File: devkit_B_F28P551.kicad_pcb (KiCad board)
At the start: 2 copper layers, 90 x 45 mm, 0 parts

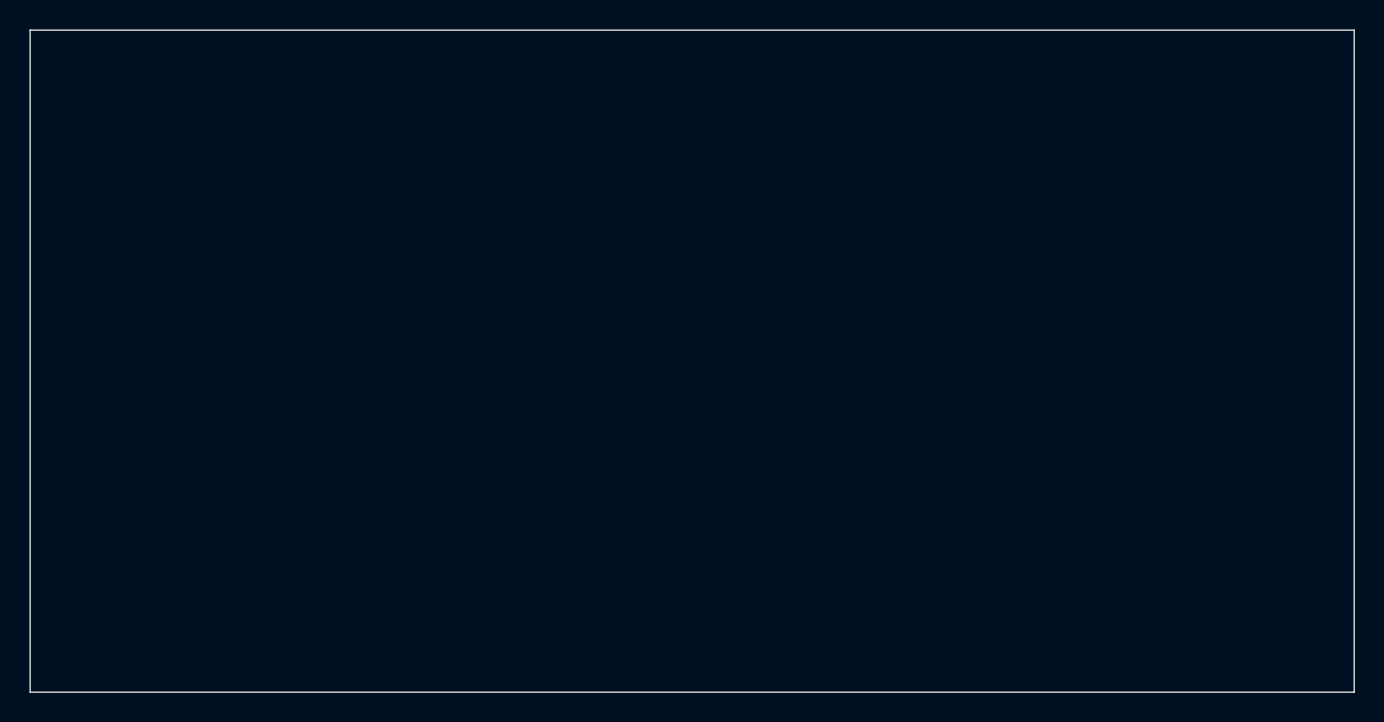
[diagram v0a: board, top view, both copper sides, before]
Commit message: spec-devkit.md devient la source de verite unique, brochage-devkit.md fusionne
La specification consolidee fournie remplace, comme elle l'annonce elle-meme,
tous les documents de brochage anterieurs. Verifiee contre
lib/C2000_Devkit_Connectors.kicad_sym: 56 positions sur 56, zero ecart.

brochage-devkit.md dupliquait desormais les memes 56 positions dans une autre
mise en forme — le mode de defaillance exact qui vient de couter trois semaines
de divergence. Il est reduit a ce qu'il avait d'unique et renomme
nappes-shield.md: les quatre nappes vers la carte de puissance, et la
repartition des cartes.

La specification apporte trois choses absentes du depot: l'entraxe 25,4 mm des
rangees (contre 22,86 mm pour l'ESP32, soit deux references de support sur le
shield), la valeur OTP BOOTPIN_CONFIG = 0x5AFF18FF, et l'obligation d'ecrire
GPIOHAMSEL pour piloter GPIO20/GPIO21 en numerique sur le F28P551.

Le contour du devkit passe de 90 x 45 a 75 x 28 mm: il portait « dimension a
confirmer », elle l'est.

Conflit non tranche, porte dans les points ouverts: la specification recommande
quatre couches pour un plan de masse continu sous la zone analogique, la
contrainte de fabrication du CLAUDE.md en pose deux.

Co-Authored-By: Claude Opus 5 <noreply@anthropic.com>
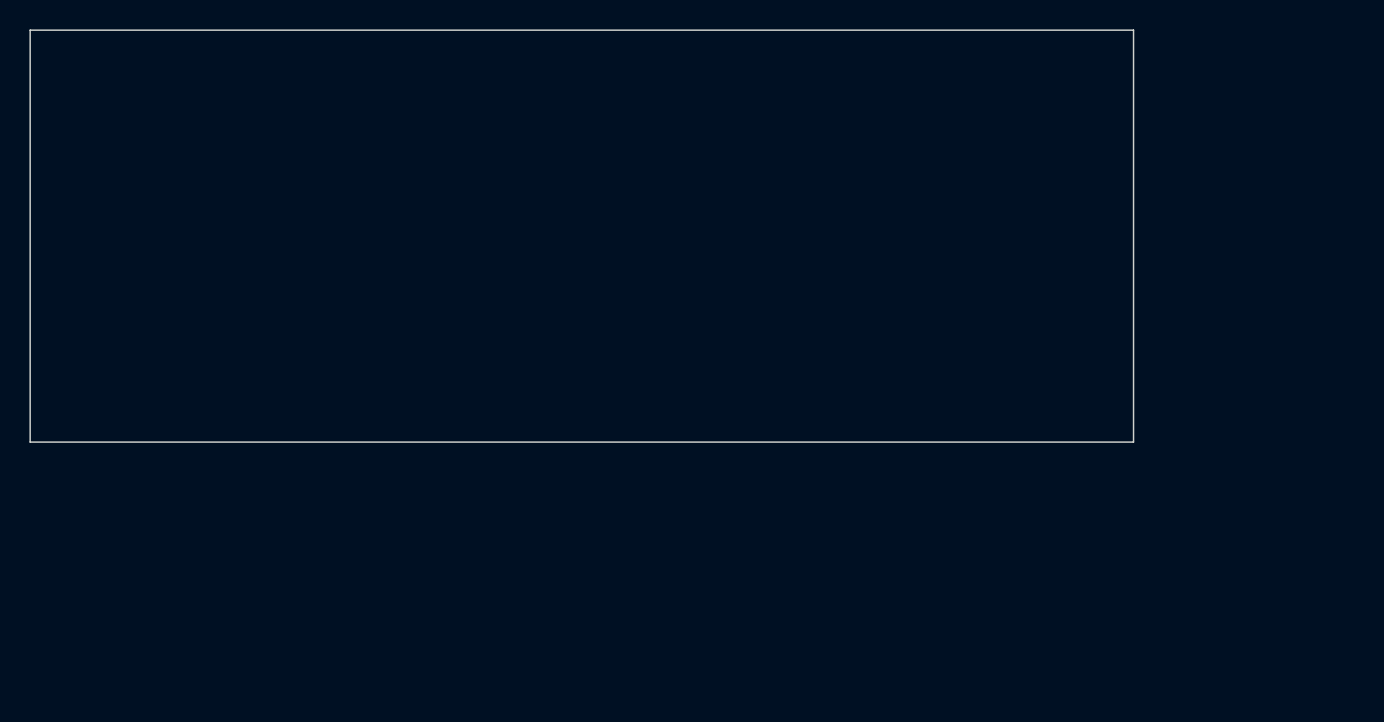
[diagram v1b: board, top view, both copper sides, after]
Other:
- board size 90 x 45 mm -> 75 x 28 mm
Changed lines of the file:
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@@
 	)
 	(net 0 "")
-	(gr_line (start 100.000 80.000) (end 190.000 80.000)
+	(gr_line (start 100.000 80.000) (end 175.000 80.000)
 		(stroke (width 0.1) (type default)) (layer "Edge.Cuts")
 	)
-	(gr_line (start 190.000 80.000) (end 190.000 125.000)
+	(gr_line (start 175.000 80.000) (end 175.000 108.000)
 		(stroke (width 0.1) (type default)) (layer "Edge.Cuts")
 	)
-	(gr_line (start 190.000 125.000) (end 100.000 125.000)
+	(gr_line (start 175.000 108.000) (end 100.000 108.000)
 		(stroke (width 0.1) (type default)) (layer "Edge.Cuts")
 	)
-	(gr_line (start 100.000 125.000) (end 100.000 80.000)
+	(gr_line (start 100.000 108.000) (end 100.000 80.000)
 		(stroke (width 0.1) (type default)) (layer "Edge.Cuts")
 	)

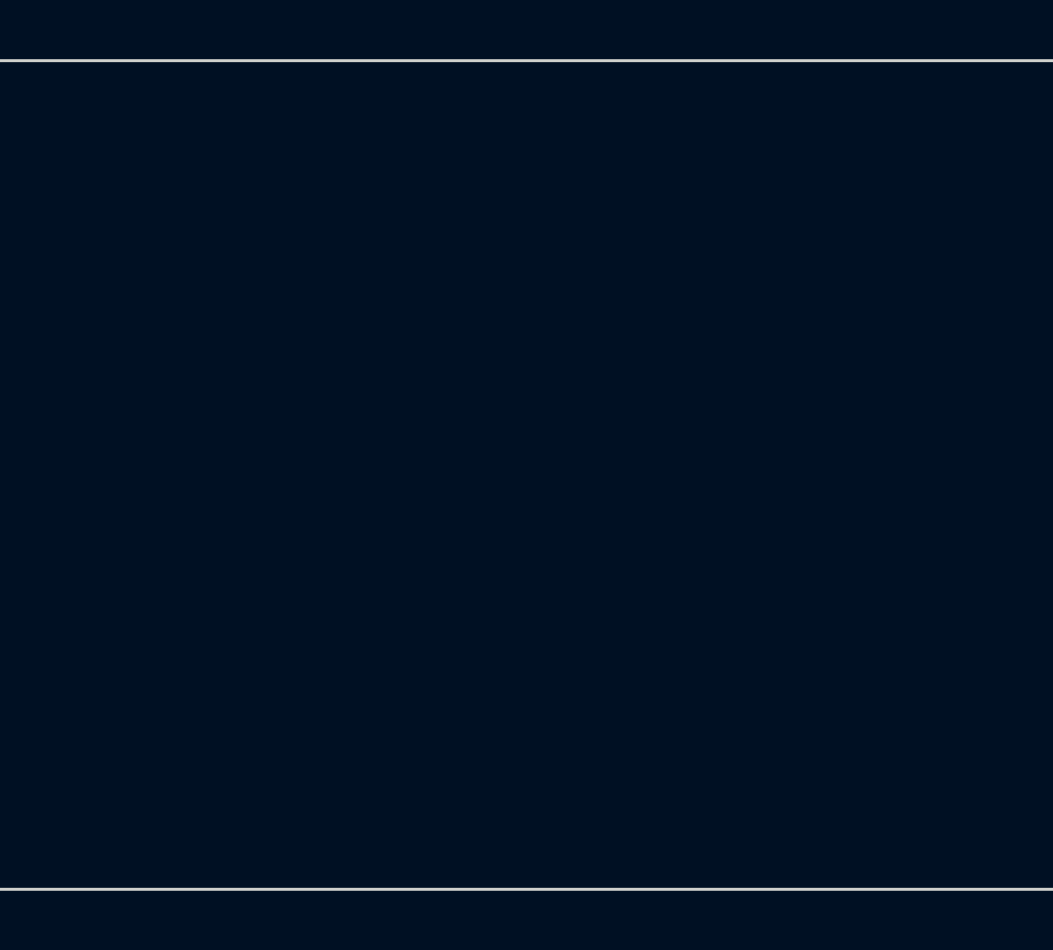
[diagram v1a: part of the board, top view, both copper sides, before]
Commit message: PCB du devkit B: 24 empreintes posees depuis le schema
Premier passage de « Mettre a jour le PCB depuis le schema ». Les composants
discrets sont la; le MCU et les deux rangees du connecteur manquent encore,
leur correction d'empreinte ayant ete ecrasee par KiCad — voir le commit
suivant.

Co-Authored-By: Claude Opus 5 <noreply@anthropic.com>
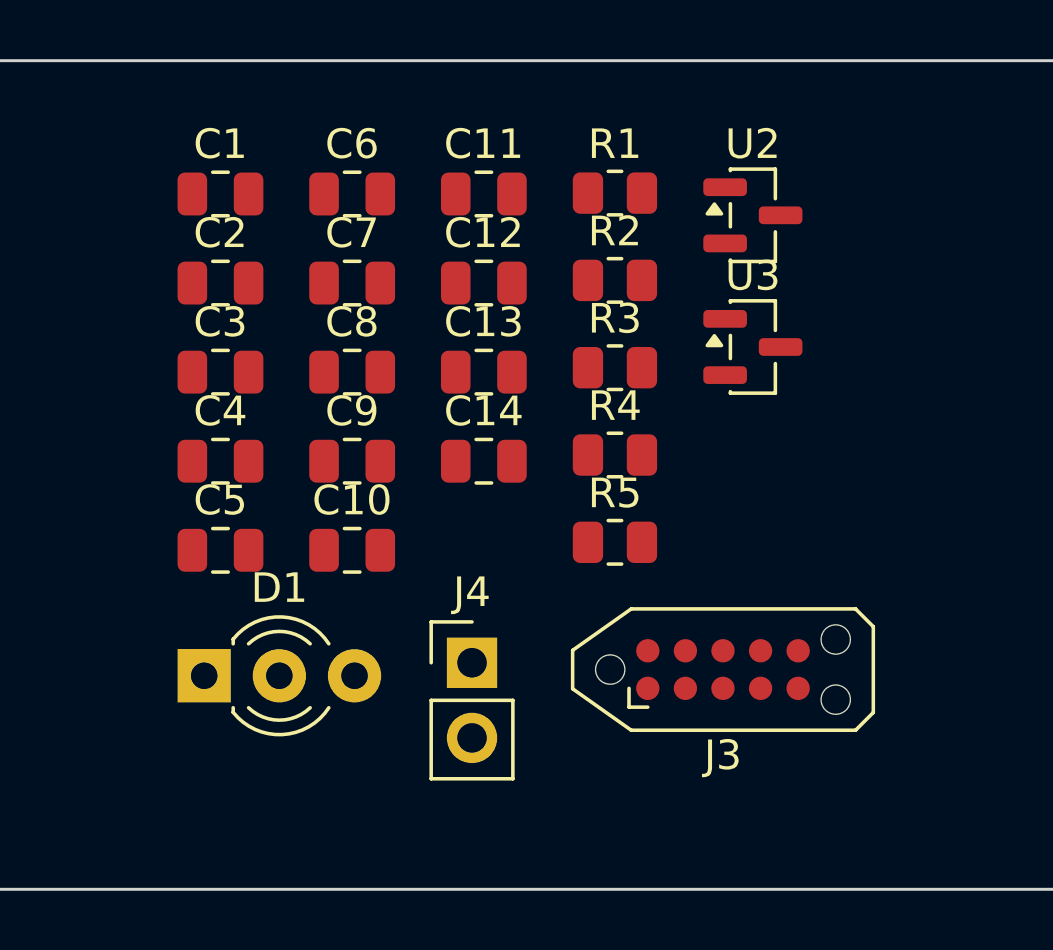
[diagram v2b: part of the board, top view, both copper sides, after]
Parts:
- added C1: 10u, Capacitor_SMD:C_0805_2012Metric, F.Cu at (121.7, 84.5)
- added C10: 100n, Capacitor_SMD:C_0805_2012Metric, F.Cu at (126.2, 96.5)
- added C11: 100n, Capacitor_SMD:C_0805_2012Metric, F.Cu at (130.6, 84.5)
- added C12: 10u, Capacitor_SMD:C_0805_2012Metric, F.Cu at (130.6, 87.5)
- added C13: 2u2, Capacitor_SMD:C_0805_2012Metric, F.Cu at (130.6, 90.5)
- added C14: 100n, Capacitor_SMD:C_0805_2012Metric, F.Cu at (130.6, 93.5)
- added C2: 10u, Capacitor_SMD:C_0805_2012Metric, F.Cu at (121.7, 87.5)
- added C3: 10u, Capacitor_SMD:C_0805_2012Metric, F.Cu at (121.7, 90.5)
- added C4: 10u, Capacitor_SMD:C_0805_2012Metric, F.Cu at (121.7, 93.5)
- added C5: 100n, Capacitor_SMD:C_0805_2012Metric, F.Cu at (121.7, 96.5)
- added C6: 100n, Capacitor_SMD:C_0805_2012Metric, F.Cu at (126.2, 84.5)
- added C7: 2u2, Capacitor_SMD:C_0805_2012Metric, F.Cu at (126.2, 87.5)
- added C8: 100n, Capacitor_SMD:C_0805_2012Metric, F.Cu at (126.2, 90.5)
- added C9: 100n, Capacitor_SMD:C_0805_2012Metric, F.Cu at (126.2, 93.5)
- added D1: LED_BICOLORE_3MM, LED_THT:LED_D3.0mm-3, F.Cu at (121.2, 100.8)
- added J3: Tag-Connect-2050_10, Connector:Tag-Connect_TC2050-IDC-NL_2x05_P1.27mm_Vertical, F.Cu at (138.7, 100.6)
- added J4: RESET, Connector_PinHeader_2.54mm:PinHeader_1x02_P2.54mm_Vertical, F.Cu at (130.2, 100.3)
- added R1: 2k2, Resistor_SMD:R_0805_2012Metric, F.Cu at (135.1, 84.5)
- added R2: 10k, Resistor_SMD:R_0805_2012Metric, F.Cu at (135.1, 87.4)
- added R3: 10k, Resistor_SMD:R_0805_2012Metric, F.Cu at (135.1, 90.4)
- added R4: 10k, Resistor_SMD:R_0805_2012Metric, F.Cu at (135.1, 93.3)
- added R5: 1k, Resistor_SMD:R_0805_2012Metric, F.Cu at (135.1, 96.3)
- added U2: MCP1700-3302E/TT, Package_TO_SOT_SMD:SOT-23, F.Cu at (139.7, 85.2)
- added U3: MCP1700-3302E/TT, Package_TO_SOT_SMD:SOT-23, F.Cu at (139.7, 89.7)

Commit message: Methode de travail KiCad + agent, et PCB du devkit B complet
Une facon de travailler inhabituelle demandait d'etre ecrite: l'agent lit les
datasheets, redige la specification, genere les symboles, pose les composants
et choisit les boitiers; le placement et le routage restent manuels.
doc/methode-kicad-claude.md garde surtout la trace des pieges de format, chacun
avec sa signature — KiCad repond « echec du chargement » et rien de plus quand
un fichier est malforme, donc reconnaitre le symptome est tout ce qui fait
gagner du temps. Plus un tableau « en cas de ».

Emporte aussi le PCB du devkit B, passe de 24 a 27 empreintes: le F8 accepte
desormais U1 et les deux rangees du connecteur, dont la propriete Footprint
etait vide sur l'instance.

DRC: 106 elements non connectes, plus des violations d'anneau, d'isolation et
de serigraphie. Attendu et sans signification a ce stade — les empreintes
arrivent empilees a l'endroit du clic, rien n'est place ni route.

Co-Authored-By: Claude Opus 5 <noreply@anthropic.com>
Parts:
- added J1: DEVKIT_C2000_ROW_A, Connector_PinHeader_2.54mm:PinHeader_1x28_P2.54mm_Vertical, F.Cu at (180.3, 52.8)
- added J2: DEVKIT_C2000_ROW_B, Connector_PinHeader_2.54mm:PinHeader_1x28_P2.54mm_Vertical, F.Cu at (184.9, 52.8)
- added U1: TMS320F28P551SG5PM, Package_QFP:LQFP-64_10x10mm_P0.5mm, F.Cu at (158.5, 94.0)

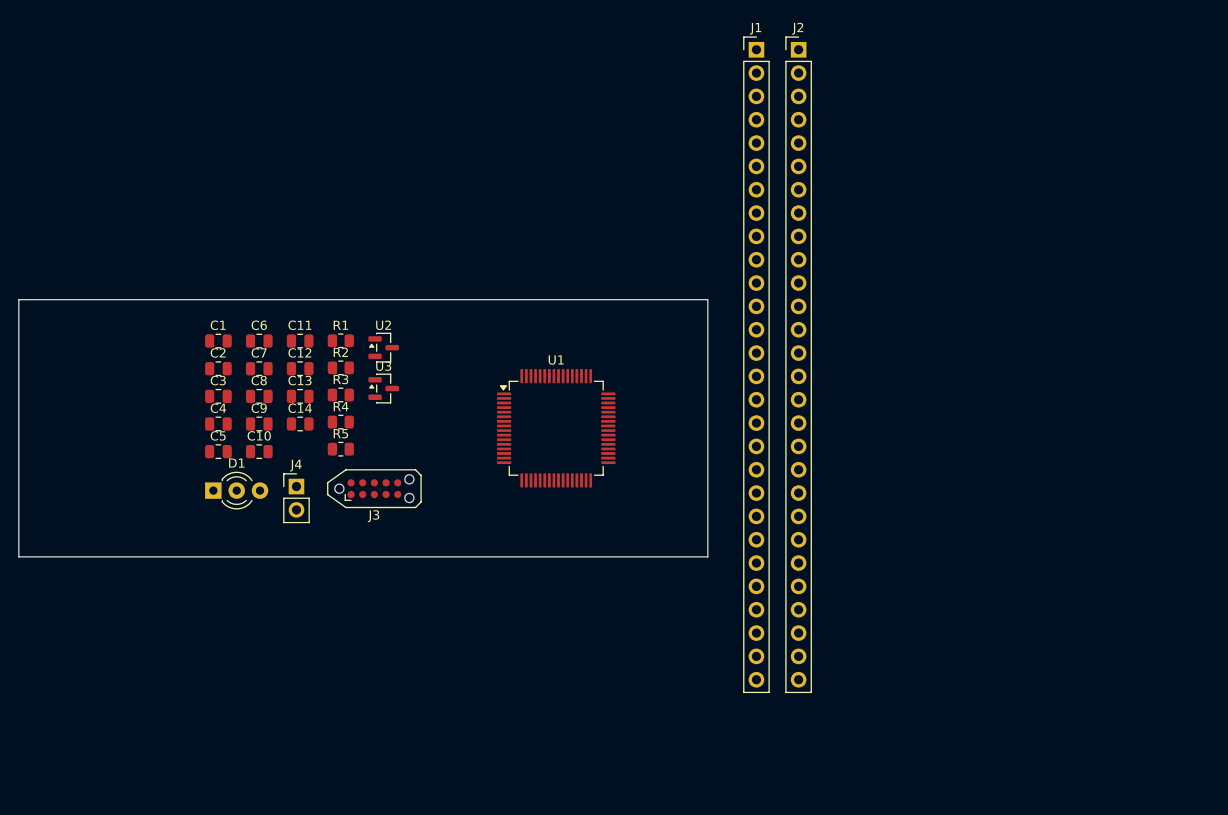
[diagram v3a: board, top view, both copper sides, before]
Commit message: PCB du devkit A peuple: 27 empreintes, les deux cartes convergent
Le F8 passe sans erreur sur le A, avec le TC2050 a la place de l'ancienne
embase. Les deux PCB portent desormais les memes 27 empreintes.

DRC identique de part et d'autre a une violation de serigraphie pres: 106
elements non connectes, 61 annular_width, ~60 clearance. Aucun n'a de sens a
ce stade — les empreintes arrivent empilees et rien n'est place ni route. Les
annular_width viennent de la confrontation entre les empreintes standard et
les regles de gravure maison (via 2 mm, percage 0,8 mm); c'est exactement la
tension que la decision 12 anticipe entre les deux variantes de fabrication.

Co-Authored-By: Claude Opus 5 <noreply@anthropic.com>
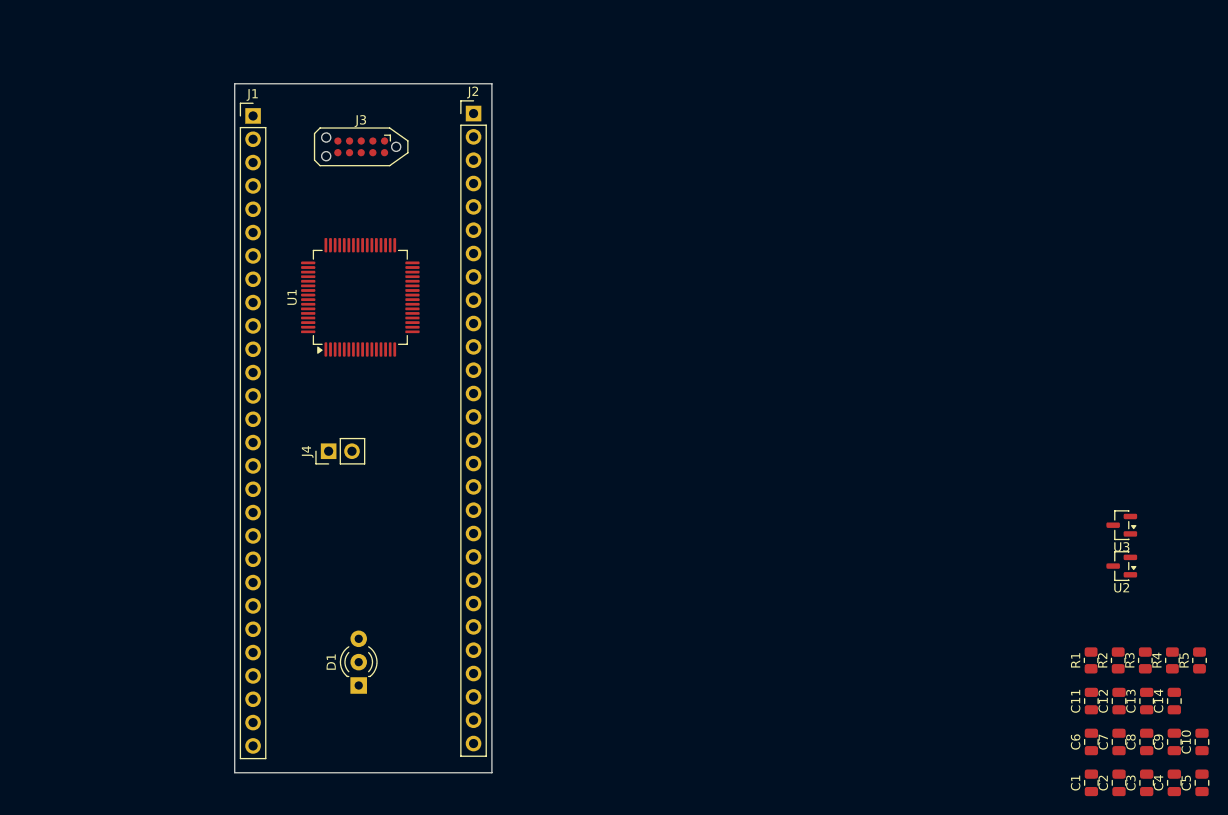
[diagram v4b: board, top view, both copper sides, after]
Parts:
- moved C5 113.0 mm to (228.8, 132.6), turned to 90 degrees
- moved C4 111.2 mm to (225.8, 132.6), turned to 90 degrees
- moved C3 109.5 mm to (222.8, 132.6), turned to 90 degrees
- moved C2 107.9 mm to (219.8, 132.6), turned to 90 degrees
- moved C10 107.4 mm to (228.8, 128.2), turned to 90 degrees
- moved C1 106.5 mm to (216.8, 132.6), turned to 90 degrees
- moved C9 105.5 mm to (225.8, 128.2), turned to 90 degrees
- moved C8 103.7 mm to (222.8, 128.2), turned to 90 degrees
- moved C7 102.0 mm to (219.8, 128.2), turned to 90 degrees
- moved C6 100.5 mm to (216.8, 128.2), turned to 90 degrees
- moved C14 99.8 mm to (225.8, 123.7), turned to 90 degrees
- moved C13 97.9 mm to (222.8, 123.7), turned to 90 degrees
- moved R5 96.3 mm to (228.5, 119.3), turned to 90 degrees
- moved C12 96.2 mm to (219.8, 123.7), turned to 90 degrees
- moved C11 94.6 mm to (216.8, 123.7), turned to 90 degrees
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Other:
- board size 75 x 28 mm -> 28 x 75 mm
